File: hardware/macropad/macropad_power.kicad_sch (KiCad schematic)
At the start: 20 parts, among them Q1 Q_PMOS, Q2 FS8205A, U6 TP4056-42-ESOP8, U7 DW01A, U8 RT8010AGQW

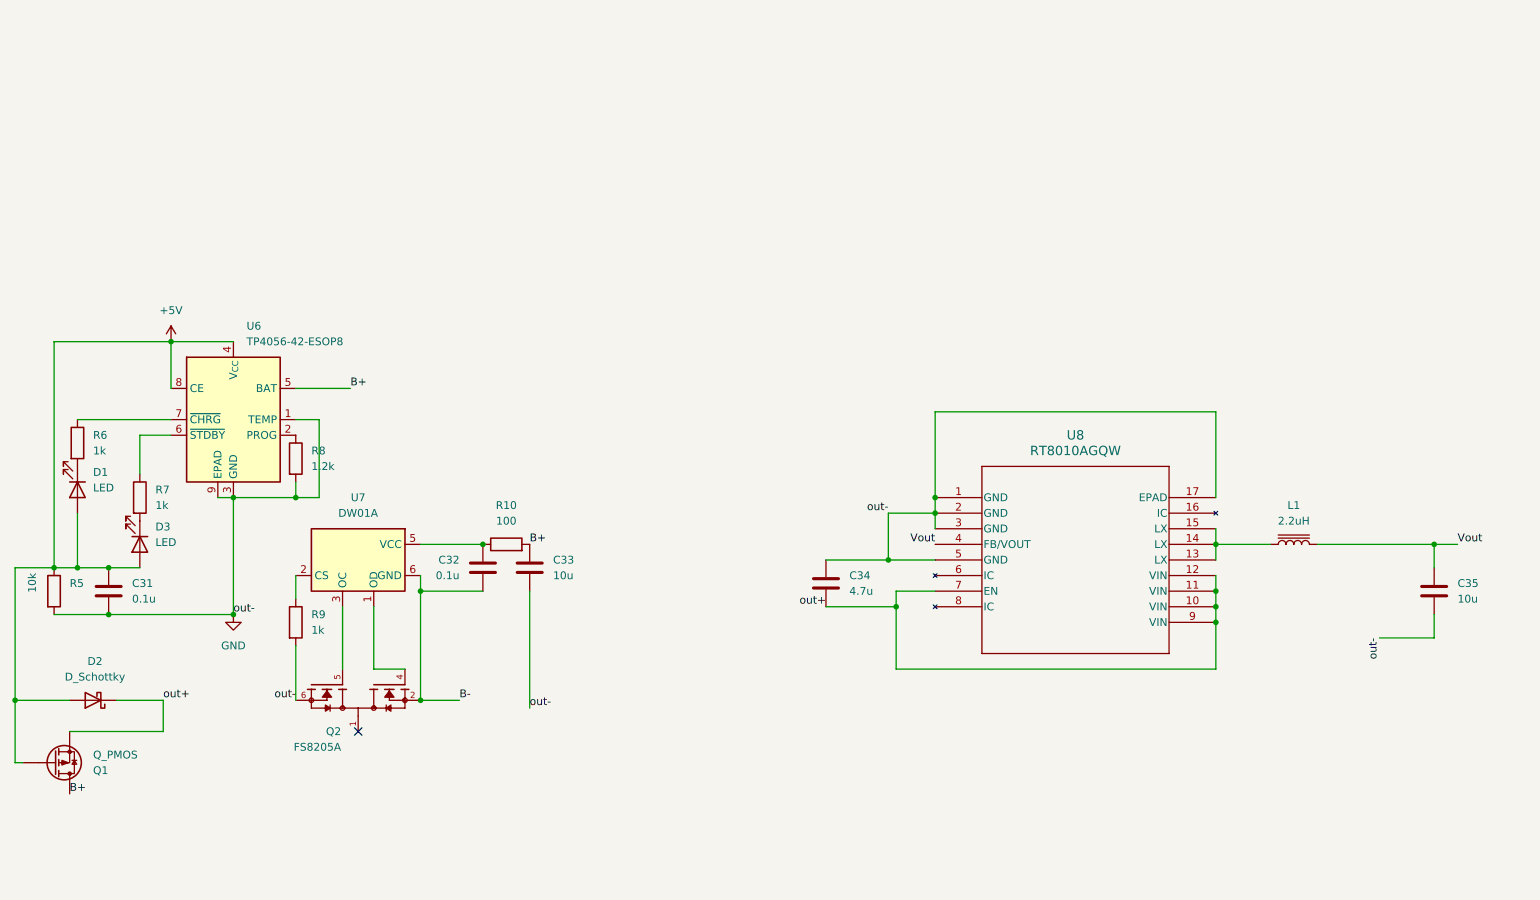
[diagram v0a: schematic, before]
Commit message: updated bat switch, added 10k resistors. fixed fps
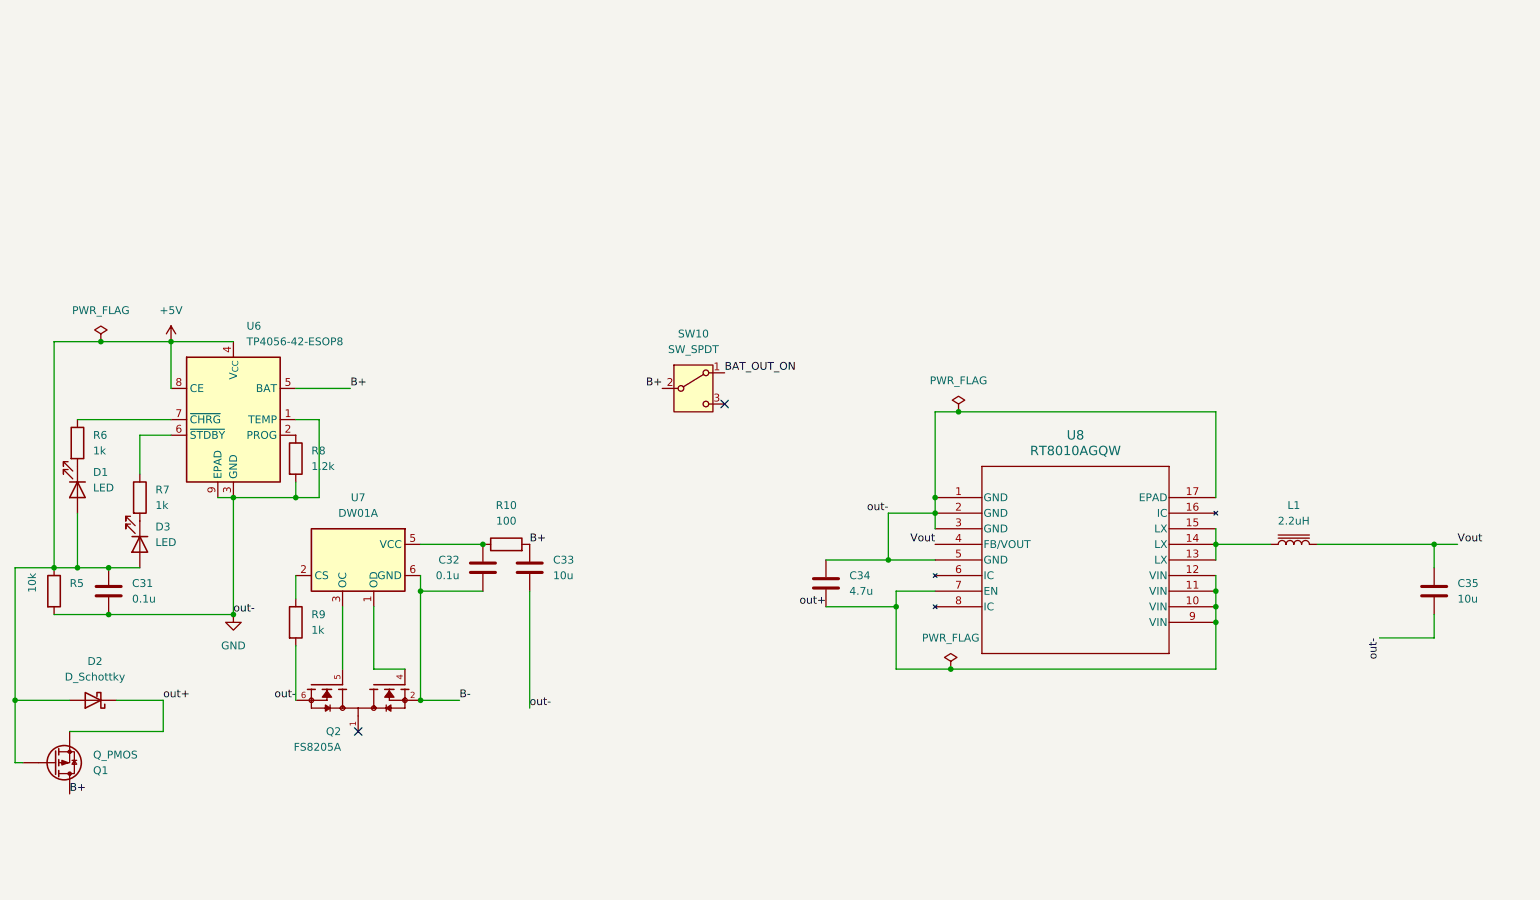
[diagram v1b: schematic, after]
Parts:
- added SW10: SW_SPDT, symbol Switch:SW_SPDT
- D2: footprint (none) -> Diode_SMD:D_SMA
- Q2: footprint (none) -> FS8205A:SOP65P640X120-8N
- R5: footprint Resistor_SMD:R_0402_1005Metric -> Resistor_SMD:R_0805_2012Metric
- U8: footprint (none) -> RT8010:WQFN16_RT8010_RIT-M
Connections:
- net B+: now also SW10.2 (B)
- new net BAT_OUT_ON: SW10.1 (A)
- no-connect marks 1 -> 2

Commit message: updated symbols. changed power. erc fixxed halfway
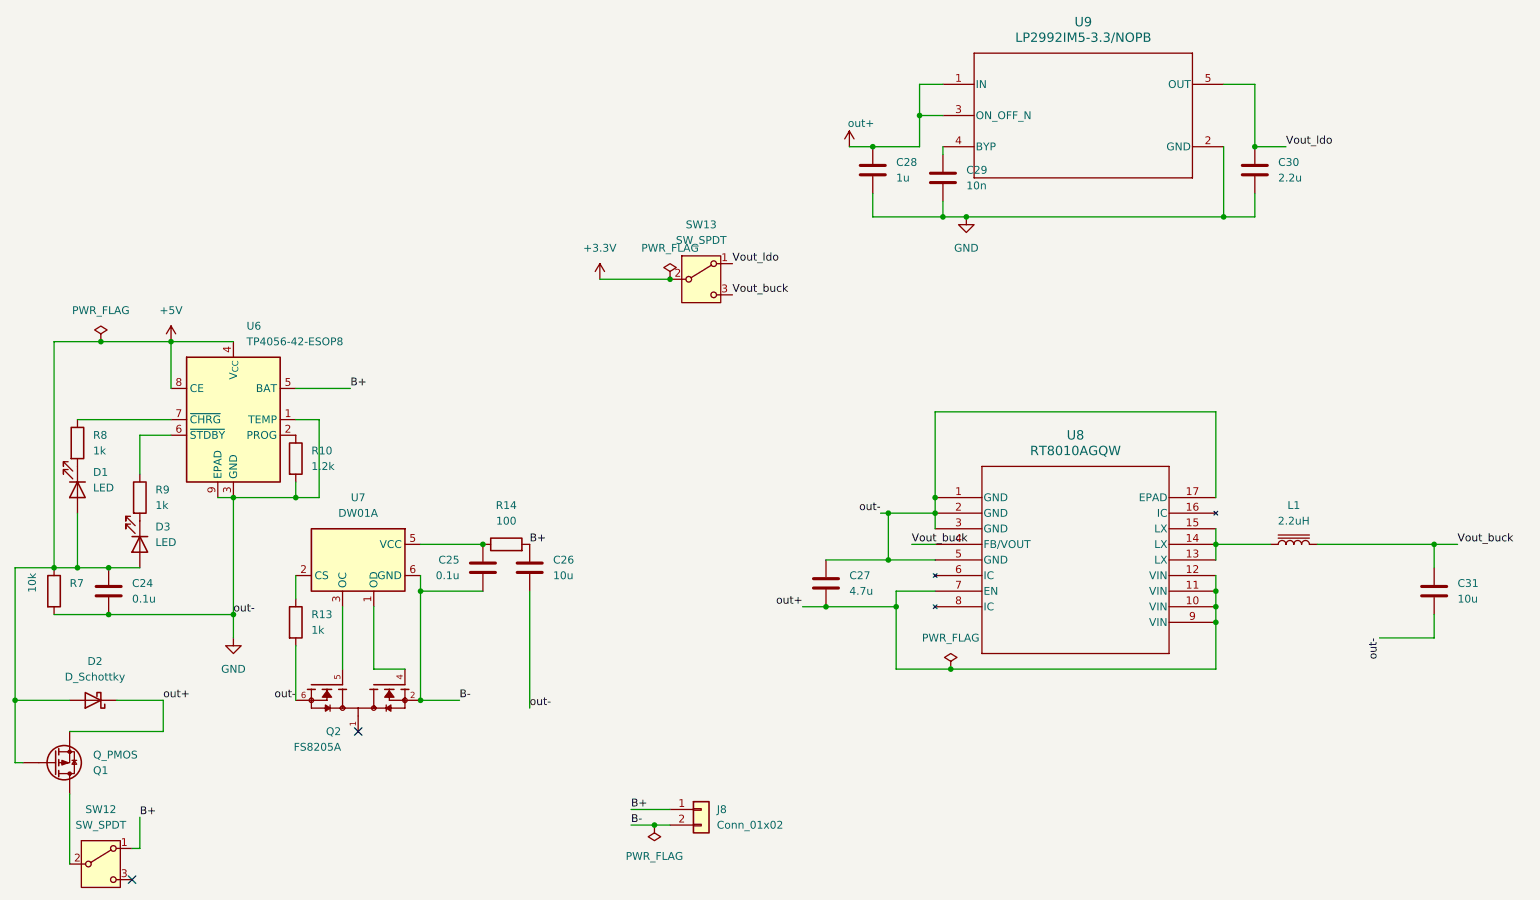
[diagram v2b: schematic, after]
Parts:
- added C28: 1u, Capacitor_SMD:C_0805_2012Metric, symbol Device:C
- added C29: 10n, Capacitor_SMD:C_0603_1608Metric, symbol Device:C
- added C30: 2.2u, Capacitor_SMD:C_0603_1608Metric, symbol Device:C
- added J8: Conn_01x02, Connector_Wire:SolderWire-0.5sqmm_1x02_P4.6mm_D0.9mm_OD2.1mm, symbol Connector_Generic:Conn_01x02
- added SW13: SW_SPDT, symbol Switch:SW_SPDT
- added U9: LP2992IM5-3.3/NOPB, LP2992:DBV0005A_N, symbol LP2992:LP2992IM5-3.3_NOPB
- renumbered C31 to C24, C32 to C25, C33 to C26, C34 to C27, C35 to C31, R8 to R10, R9 to R13, R10 to R14, R5 to R7, R6 to R8, R7 to R9, SW10 to SW12
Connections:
- net BAT_OUT_ON is gone; now on net B+: SW12.1 (A)
- net B+: now also J8.1 (Pin_1); no longer Q1.D, SW12.2 (B)
- net B-: now also J8.2 (Pin_2)
- net GND: now also C28.2, C29.2, C30.2, U9.2 (GND)
- net out+: now also C28.1, U9.1 (IN), U9.3 (ON_OFF_N)
- net Vout renamed Vout_buck
- net Vout_buck: now also SW13.3 (C)
- new net: C29.1, U9.4 (BYP)
- new net: Q1.D, SW12.2 (B)
- new net +3.3V: SW13.2 (B)
- new net Vout_ldo: C30.1, SW13.1 (A), U9.5 (OUT)
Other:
- moved on the sheet: SW12

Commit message: erc for power checked
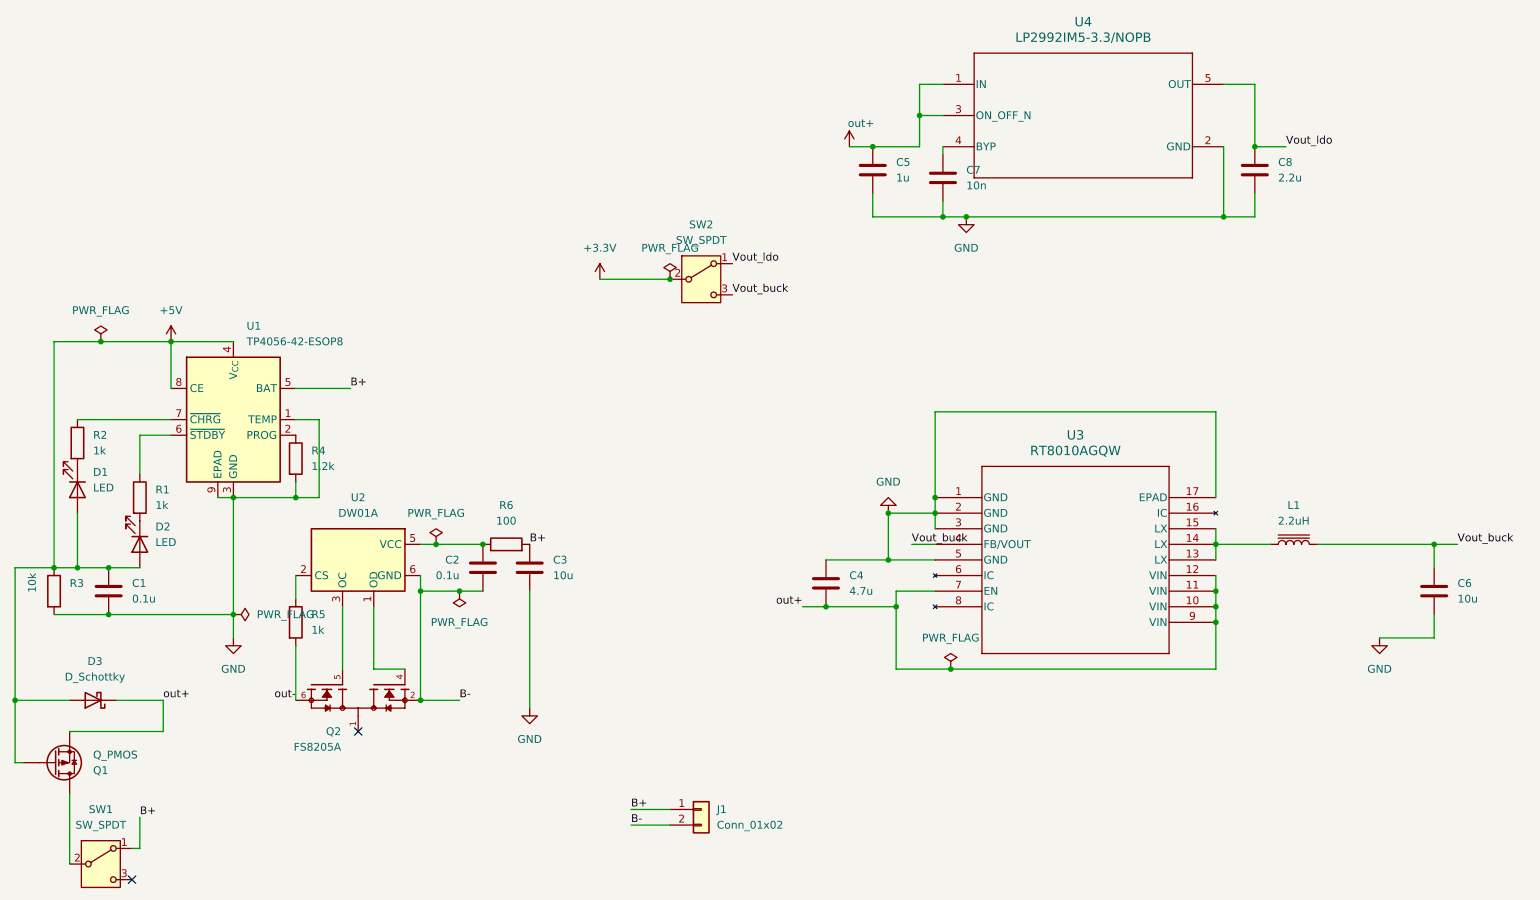
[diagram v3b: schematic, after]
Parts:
- renumbered C24 to C1, C25 to C2, C26 to C3, C27 to C4, C28 to C5, C31 to C6, C29 to C7, C30 to C8, D3 to D2, D2 to D3, J8 to J1, R9 to R1, R8 to R2, R7 to R3, R10 to R4, R13 to R5, R14 to R6, SW12 to SW1, SW13 to SW2, U6 to U1, U7 to U2, U8 to U3, U9 to U4
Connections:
- net GND: no longer Q2.6, Q2.7, R5.2
- new net out-: Q2.6, Q2.7, R5.2

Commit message: erc for macropad checked
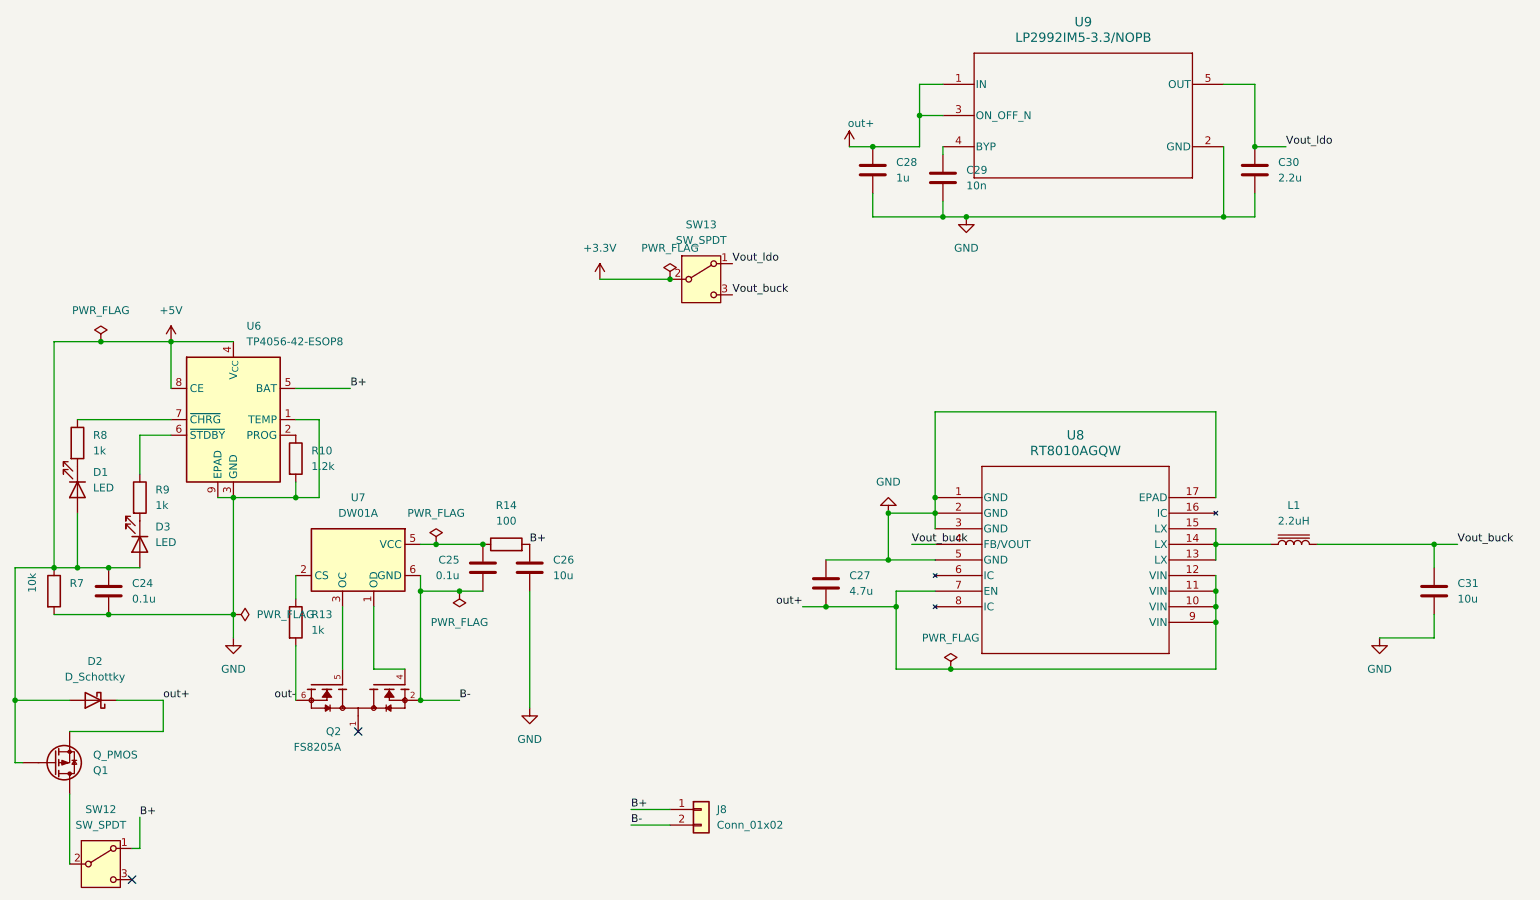
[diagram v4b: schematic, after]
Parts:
- renumbered C1 to C24, C2 to C25, C3 to C26, C4 to C27, C5 to C28, C7 to C29, C8 to C30, C6 to C31, D3 to D2, D2 to D3, J1 to J8, R4 to R10, R5 to R13, R6 to R14, R3 to R7, R2 to R8, R1 to R9, SW1 to SW12, SW2 to SW13, U1 to U6, U2 to U7, U3 to U8, U4 to U9

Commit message: updated symbols. all erc passed
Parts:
- removed U8: RT8010AGQW, RT8010:WQFN16_RT8010_RIT-M, symbol 2026-02-28_18-02-32:RT8010AGQW
- added U8: RT8010AGQW, RT8010:WQFN16_RT8010_RIT, symbol RT8010:RT8010AGQW
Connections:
- net GND: now also U8.1 (GND), U8.17 (EPAD), U8.2 (GND), U8.3 (GND), U8.5 (GND)
- net Vout_buck: now also U8.4 (FB/VOUT)
- net out+: now also U8.10 (VIN), U8.11 (VIN), U8.12 (VIN), U8.7 (EN), U8.9 (VIN)
- net at L1.1: now also U8.13 (LX), U8.14 (LX), U8.15 (LX)
- no-connect marks 2 -> 4

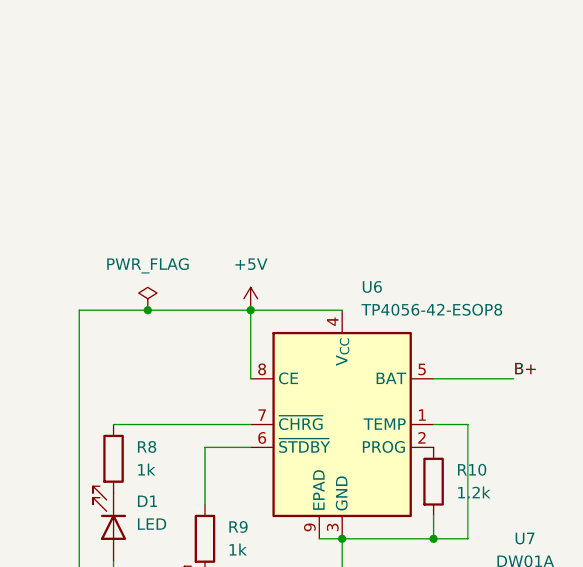
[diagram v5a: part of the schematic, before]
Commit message: added usba fp, updated pcb, 5v to vbus
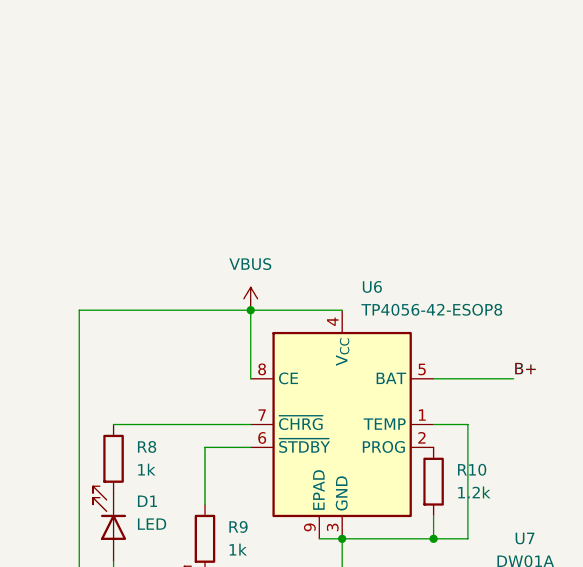
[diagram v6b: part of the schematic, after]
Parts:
- SW12, SW13: footprint (none) -> Button_Switch_THT:SW_Slide_SPDT_Angled_CK_OS102011MA1Q
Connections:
- net +5V renamed VBUS
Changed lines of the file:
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@@
 	)
 	(junction
-		(at 104.14 96.52)
-		(diameter 0)
-		(color 0 0 0 0)
-	)
-	(junction
 		(at 232.41 132.08)
 		(diameter 0)
@@
 	(wire
 		(pts
-			(xy 115.57 96.52) (xy 104.14 96.52)
+			(xy 96.52 96.52) (xy 115.57 96.52)
 		)
 		(stroke
@@
 	(wire
 		(pts
-			(xy 104.14 96.52) (xy 96.52 96.52)
-		)
-		(stroke
-			(width 0)
-			(type default)
-		)
-	)
-	(wire
-		(pts
 			(xy 148.59 139.7) (xy 148.59 149.86)
 		)
@@
 			)
 		)
-		(property "Footprint" ""
+		(property "Footprint" "Button_Switch_THT:SW_Slide_SPDT_Angled_CK_OS102011MA1Q"
 			(at 104.14 181.61 0)
 			(effects
@@
 	)
 	(symbol
-		(lib_id "power:PWR_FLAG")
-		(at 104.14 96.52 0)
-		(unit 1)
-		(exclude_from_sim no)
-		(in_bom yes)
-		(on_board yes)
-		(dnp no)
-		(fields_autoplaced yes)
-		(property "Reference" "#FLG02"
-			(at 104.14 94.615 0)
-			(effects
-				(font
-					(size 1.27 1.27)
-				)
-				(hide yes)
-			)
-		)
-		(property "Value" "PWR_FLAG"
-			(at 104.14 91.44 0)
-			(effects
-				(font
-					(size 1.27 1.27)
-				)
-			)
-		)
-		(property "Footprint" ""
-			(at 104.14 96.52 0)
-			(effects
-				(font
-					(size 1.27 1.27)
-				)
-				(hide yes)
-			)
-		)
-		(property "Datasheet" "~"
-			(at 104.14 96.52 0)
-			(effects
-				(font
-					(size 1.27 1.27)
-				)
-				(hide yes)
-			)
-		)
-		(property "Description" "Special symbol for telling ERC where power comes from"
-			(at 104.14 96.52 0)
-			(effects
-				(font
-					(size 1.27 1.27)
-				)
-				(hide yes)
-			)
-		)
-		(pin "1"
-		)
-		(instances
-			(project "macropad_power"
-				(path "/228dc472-b306-4e5f-8dc5-2bf23eb4978d"
-					(reference "#FLG01")
-					(unit 1)
-				)
-				(path "/228dc472-b306-4e5f-8dc5-2bf23eb4978d/5b38d27c-d7f4-4a8d-8a5e-966bba03fead"
-					(reference "#FLG02")
-					(unit 1)
-				)
-			)
-		)
-	)
-	(symbol
 		(lib_id "Device:LED")
 		(at 110.49 129.54 270)
@@
 	)
 	(symbol
-		(lib_id "power:+5V")
-		(at 115.57 96.52 0)
-		(unit 1)
-		(exclude_from_sim no)
-		(in_bom yes)
-		(on_board yes)
-		(dnp no)
-		(fields_autoplaced yes)
-		(property "Reference" "#PWR06"
-			(at 115.57 100.33 0)
-			(effects
-				(font
-					(size 1.27 1.27)
-				)
-				(hide yes)
-			)
-		)
-		(property "Value" "+5V"
-			(at 115.57 91.44 0)
-			(effects
-				(font
-					(size 1.27 1.27)
-				)
-			)
-		)
-		(property "Footprint" ""
-			(at 115.57 96.52 0)
-			(effects
-				(font
-					(size 1.27 1.27)
-				)
-				(hide yes)
-			)
-		)
-		(property "Datasheet" ""
-			(at 115.57 96.52 0)
-			(effects
-				(font
-					(size 1.27 1.27)
-				)
-				(hide yes)
-			)
-		)
-		(property "Description" "Power symbol creates a global label with name \"+5V\""
-			(at 115.57 96.52 0)
-			(effects
-				(font
-					(size 1.27 1.27)
-				)
-				(hide yes)
-			)
-		)
-		(pin "1"
-		)
-		(instances
-			(project ""
-				(path "/228dc472-b306-4e5f-8dc5-2bf23eb4978d"
-					(reference "#PWR01")
-					(unit 1)
-				)
-				(path "/228dc472-b306-4e5f-8dc5-2bf23eb4978d/5b38d27c-d7f4-4a8d-8a5e-966bba03fead"
-					(reference "#PWR06")
-					(unit 1)
-				)
-			)
-		)
-	)
-	(symbol
 		(lib_id "Battery_Management:DW01A")
 		(at 146.05 132.08 0)
@@
 	)
 	(symbol
+		(lib_id "power:VBUS")
+		(at 115.57 96.52 0)
+		(unit 1)
+		(exclude_from_sim no)
+		(in_bom yes)
+		(on_board yes)
+		(dnp no)
+		(fields_autoplaced yes)
+		(property "Reference" "#PWR06"
+			(at 115.57 100.33 0)
+			(effects
+				(font
+					(size 1.27 1.27)
+				)
+				(hide yes)
+			)
+		)
+		(property "Value" "VBUS"
+			(at 115.57 91.44 0)
+			(effects
+				(font
+					(size 1.27 1.27)
+				)
+			)
+		)
+		(property "Footprint" ""
+			(at 115.57 96.52 0)
+			(effects
+				(font
+					(size 1.27 1.27)
+				)
+				(hide yes)
+			)
+		)
+		(property "Datasheet" ""
+			(at 115.57 96.52 0)
+			(effects
+				(font
+					(size 1.27 1.27)
+				)
+				(hide yes)
+			)
+		)
+		(property "Description" "Power symbol creates a global label with name \"VBUS\""
+			(at 115.57 96.52 0)
+			(effects
+				(font
+					(size 1.27 1.27)
+				)
+				(hide yes)
+			)
+		)
+		(pin "1"
+		)
+		(instances
+			(project ""
+				(path "/228dc472-b306-4e5f-8dc5-2bf23eb4978d"
+					(reference "#PWR01")
+					(unit 1)
+				)
+				(path "/228dc472-b306-4e5f-8dc5-2bf23eb4978d/5b38d27c-d7f4-4a8d-8a5e-966bba03fead"
+					(reference "#PWR06")
+					(unit 1)
+				)
+			)
+		)
+	)
+	(symbol
 		(lib_id "power:VDD")
 		(at 226.06 64.77 0)
@@
 			)
 		)
-		(property "Footprint" ""
+		(property "Footprint" "Button_Switch_THT:SW_Slide_SPDT_Angled_CK_OS102011MA1Q"
 			(at 201.93 86.36 0)
 			(effects
